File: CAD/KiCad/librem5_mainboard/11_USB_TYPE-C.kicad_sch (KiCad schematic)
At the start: 131 parts, among them J12 BTB40-0.35-KYOCERA5857, Q1602 MOSFET_P, T1 TPD1E05U06, T2 TPD1E05U06, U10 PCMF2USB3S_10P, U13 PCMF2USB3S_10P, U147 MX25L1606E, U18 PCMF1USB3S_5P, U27 TPS65983B, U30 HD3SS460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

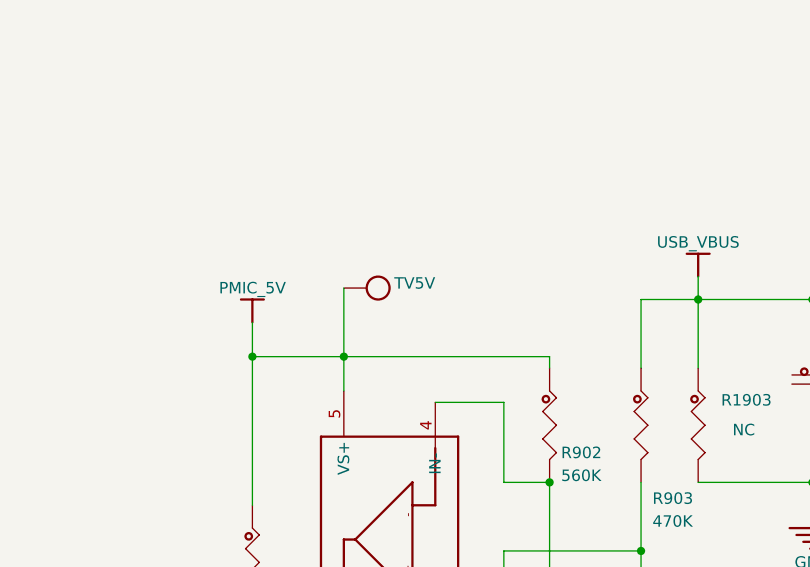
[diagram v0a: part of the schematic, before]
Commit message: Update the KiCad projects to v9.0
Signed-off-by: Eric Kuzmenko <eric.kuzmenko@puri.sm>
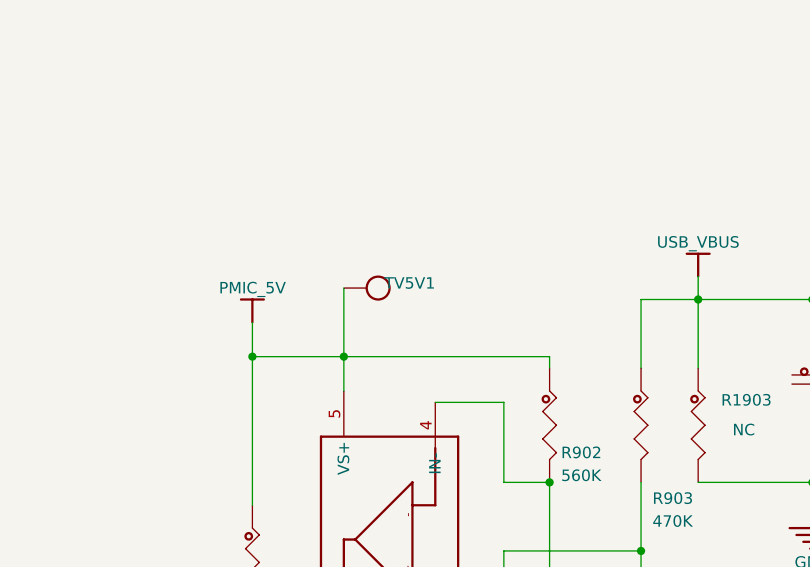
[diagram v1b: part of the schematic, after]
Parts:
- renumbered TV5V to TV5V1

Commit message: Use KiCad's new PADS importer/converter tool to go directly from PADS ascii to KiCad 10, place this newly converted project in CAD/PADS/librem5_mainboard/librem5_mainboard_kicad_conversion/, keep the previous converted project that's in CAD/KiCad/librem5_mainboard/ and update it to also use KiCad 10
The one in CAD/KiCad/ seems to be a bit better but this newly converted
project is available in case it might have some improvements (e.g. in
cross-probing or some other more accurate details). Either one (or both)
may be used to completely move the project over to KiCad.

Signed-off-by: Eric Kuzmenko <eric.kuzmenko@puri.sm>
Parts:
- C232, C233, C234, C287, C518, C519, C55: value C0603 -> 10UF; DESCRIPTION CAP CER 10uF 35V 20% X5R 0603 -> (none); VALUE 10UF -> (none)
- C235, C237, C315, C376, C378: value C0402 -> 224; DESCRIPTION CAP CER 0.22uF 35V 20% X5R 0402 -> (none); VALUE 224 -> (none)
- C236, C316: value C0201 -> 103; DESCRIPTION CAP CER 0.01uF 25V 20% X5R 0201 -> (none); VALUE 103 -> (none)
- C238, C241, C242: value C0402 -> 4.7UF; DESCRIPTION CAP CER 4.7uF 6V3 20% X5R 0402 -> (none); VALUE 4.7UF -> (none)
- C240: value C0603 -> 22UF; DESCRIPTION CAP CER 22uF 6V3 20% X5R 0603 -> (none); VALUE 22UF -> (none)
- C243, C370, C393, C514, C516, C517: value C0201 -> 105; DESCRIPTION CAP CER 1uF 6V3 20% X5R 0201 -> (none); VALUE 105 -> (none)
- C261, C262, C263, C264, C265, C266, C267, C268, C361, C362, C367, C368: value C0201 -> 0; DESCRIPTION Resistor Chip 0201 0R Ohm 1/16W 1% RALEC -> (none); VALUE 0 -> (none)
- C343, C377: value C0201 -> 220PF; DESCRIPTION CAP CER 180PF 6V3 20% NPO 0201 -> (none); VALUE 220PF -> (none)
- C369, C371, C372, C373, C374: value C0201 -> 104; DESCRIPTION CAP CER 0.1uF 6V3 20% X5R 0201 -> (none); VALUE 104 -> (none)
- C375: value C0402 -> 225; DESCRIPTION CAP CER 2.2uF 35V 20% X5R 0402 -> (none); VALUE 225 -> (none)
- C379, C380: value C0201 -> 104; DESCRIPTION CAP CER 1uF 6V3 20% X5R 0201 -> (none); VALUE 104 -> (none)
- D25: VALUE NSR20F30NXT5G -> (none)
- J12: value BTB40-0.35-KYOCERA5857 -> 24-5857-040; DESCRIPTION SOCKET BTB Ä¸×ù 0.35mm 40pin ºÏ¸ß0.7mm 5857ÏµÁÐ -> (none); VALUE 24-5857-040 -> (none)
- L24, L33: value BEAD-0402 -> 10 / HPZ1005U121-1R1TF; DESCRIPTION Resistor Chip 0402 10 Ohm 1/16W 1% RALEC -> (none); VALUE 10 / HPZ1005U121-1R1TF -> (none)
- L38, L57, L82: value BEAD-0402 -> HPZ1005U121-1R1TF; DESCRIPTION FB 120ohm@100MHz 100ohm@1GHz DCR0.13ohm 1.1A T:0.5mm -> (none); VALUE HPZ1005U121-1R1TF -> (none)
- L62, L63: value BEAD-0402 -> MZAH1005F352-R27TF; DESCRIPTION FB 3500ohm@100MHz 1600ohm@1GHz DCR1ohm 270mA T:0.5mm -> (none); VALUE MZAH1005F352-R27TF -> (none)
- L9: value BEAD-4030 -> PZ3216D600-4R0TF; DESCRIPTION Z FB 60ohm@100MHz DCR20mohm 4A T:0.85mm -> (none); VALUE PZ3216D600-4R0TF -> (none)
- Q1602: value MOSFET_P -> NTR2101PT1G; DESCRIPTION TRAN PMOS POWER 79m OHM@-1.8V DRIVE -8V SOT23 -> (none); VALUE NTR2101PT1G -> (none)
- R100, R103: value RES_2 -> 100K; DESCRIPTION Resistor Chip 0201 10K Ohm 1/16W 1% RALEC -> (none); VALUE 100K -> (none)
- R110: value RES_2 -> NC; DESCRIPTION Z Resistor Chip 0201 10K Ohm 1/16W 1% RALEC -> (none); VALUE NC -> (none)
- R111, R197, R238, R28, R45, R73, R74, R75, R76, R77, R78, R79, R80, R81, R940, R941: value RES_2 -> 0; DESCRIPTION Resistor Chip 0201 0R Ohm 1/16W 1% RALEC -> (none); VALUE 0 -> (none)
- R143, R147, R151, R155, R242, R243, R248: value RES_2 -> 10K; DESCRIPTION Resistor Chip 0201 10K Ohm 1/16W 1% RALEC -> (none); VALUE 10K -> (none)
- R153: value RES_2 -> NC; DESCRIPTION Z Resistor Chip 0201 0R Ohm 1/16W 1% RALEC -> (none); VALUE NC -> (none)
- R154: value CURRENT_R -> NC; DESCRIPTION Z -> (none); VALUE NC -> (none)
- R181, R211: value RES_2 -> 33; DESCRIPTION Resistor Chip 0201 33R Ohm 1/16W 1% RALEC -> (none); VALUE 33 -> (none)
- R1903, R63, R64: value RES_2 -> NC; DESCRIPTION Resistor Chip 0201 10K Ohm 1/16W 1% RALEC -> (none); VALUE NC -> (none)
- R223, R244, R245, R35, R36, R904, R933, R934: value RES_2 -> 100K; DESCRIPTION Resistor Chip 0201 100K Ohm 1/16W 1% RALEC -> (none); VALUE 100K -> (none)
- R251, R252: value RES_2 -> 1M; DESCRIPTION Resistor Chip 0201 1M Ohm 1/20W 1% RALEC -> (none); VALUE 1M -> (none)
- R255: value RES_2 -> 0; DESCRIPTION Resistor Chip 0201 0 Ohm 1/20W 1% RALEC -> (none); VALUE 0 -> (none)
- R54: value RES_2 -> 1M; DESCRIPTION Resistor Chip 0201 1M Ohm 1/16W 1% RALEC -> (none); VALUE 1M -> (none)
- R82: value R_0.1% -> 15K 0.1%; DESCRIPTION Resistor Chip 0402 15K Ohm 1/10W 0.1% RALEC -> (none); VALUE 15K 0.1% -> (none)
- R902: value RES_2 -> 560K; DESCRIPTION Resistor Chip 0201 560K Ohm 1/16W 1% RALEC -> (none); VALUE 560K -> (none)
- R903: value RES_2 -> 470K; DESCRIPTION Resistor Chip 0201 470K Ohm 1/16W 1% RALEC -> (none); VALUE 470K -> (none)
- T1, T2: VALUE TPD1E05U06 -> (none)
- TP1, TP108, TP109, TP110, TP111, TP112, TP113, TP114, TP115, TP19, TP51, TV1, TV34, TV35, TV7: value TEST-POINT -> M3; DESCRIPTION Z -> (none); VALUE M3 -> (none)
- TV5V1: value T_POINT_R -> (none); DESCRIPTION Z -> (none)
- U10, U13: value PCMF2USB3S_10P -> PCMF2USB3S; DESCRIPTION IC EMI FILTER FOR DIFF CH W/ ESD PROTECTION 5V WLCSP10 -> (none); VALUE PCMF2USB3S -> (none)
- U147: value MX25L1606E -> W25Q16JVUXIM; DESCRIPTION IC 3V 16Mbit SPI FLASH -> (none); VALUE W25Q16JVUXIM -> (none)
- U18, U6: value PCMF1USB3S_5P -> PCMF1USB3S; DESCRIPTION IC EMI FILTER FOR DIFF CH W/ ESD PROTECTION 5V WLCSP5 -> (none); VALUE PCMF1USB3S -> (none)
- U27: value TPS65983B -> TPS65982; DESCRIPTION IC USB PD PHY and Power Switch -> (none); VALUE TPS65982 -> (none)
- U30: DESCRIPTION IC USB TYPE-C Alternate Mode MUX IC -> (none); VALUE HD3SS460 -> (none)
- U909: value TLV3201 -> TLV3201AIDCK; DESCRIPTION IC MicroPower Push-Pull Comparators 2.7V-5.5V SC70-5 -> (none); VALUE TLV3201AIDCK -> (none)
